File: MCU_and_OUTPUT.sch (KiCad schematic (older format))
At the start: 36 parts, among them P5 CONN_5, P6 CONN_01X04, Q2 BC817-40, Q3 BC817-40, Q4 BC807-40, Q5 IRF540, Q6 BC817-40, SW1 SPST, U2 STM32F030K6, U3 LM358

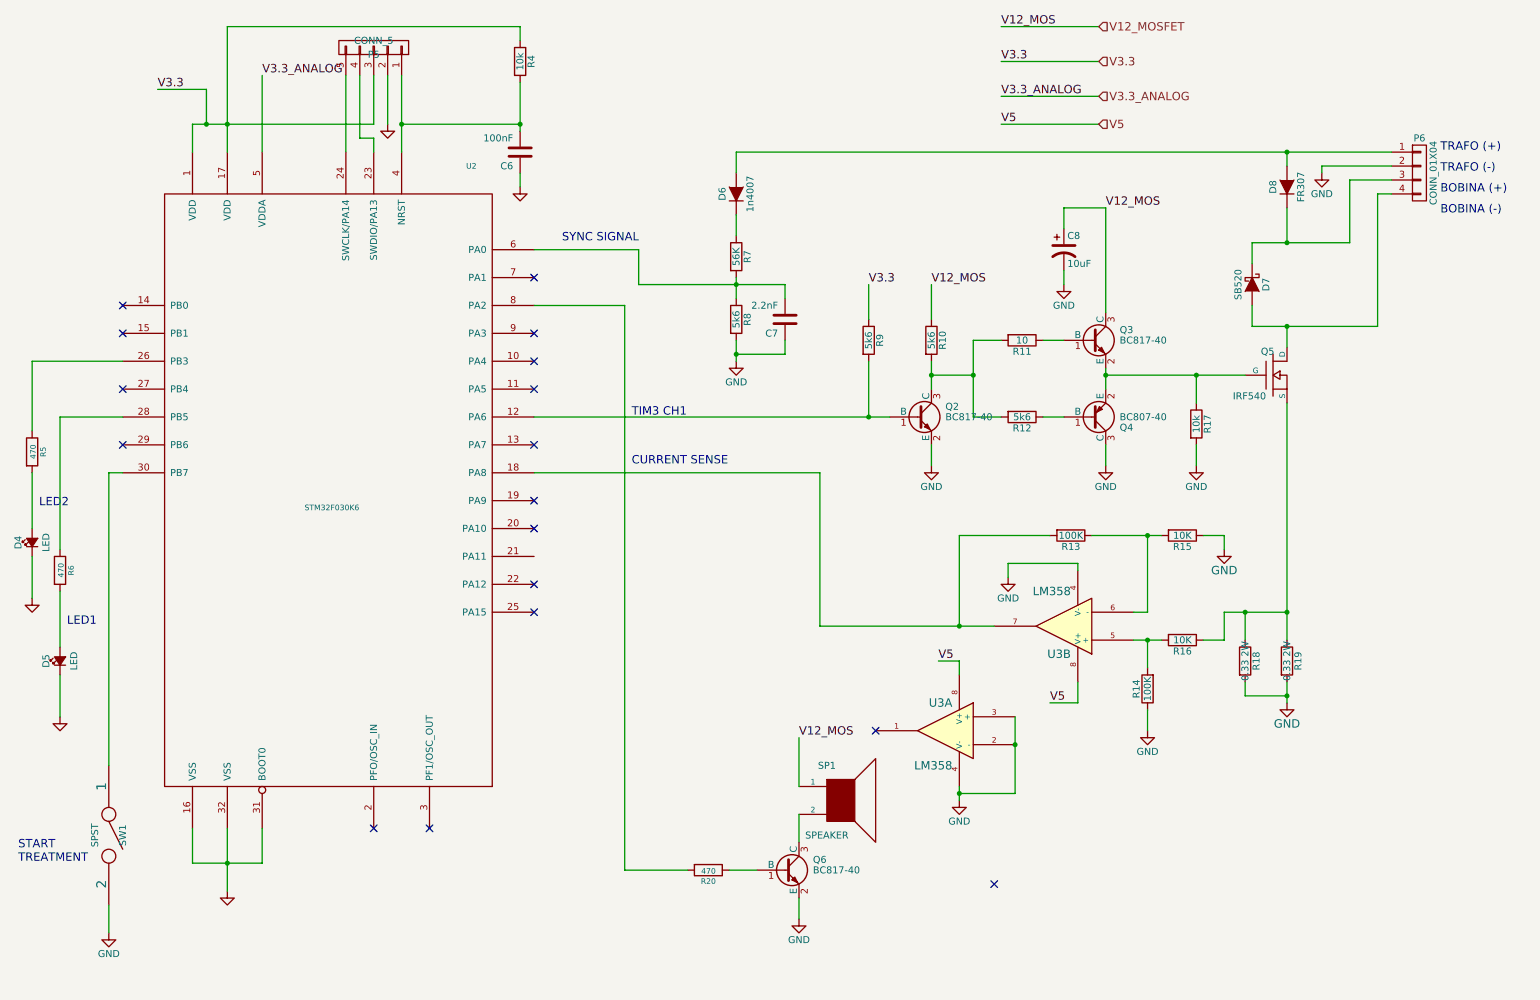
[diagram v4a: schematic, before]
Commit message: mejor ruteo, faltan 3 pistas
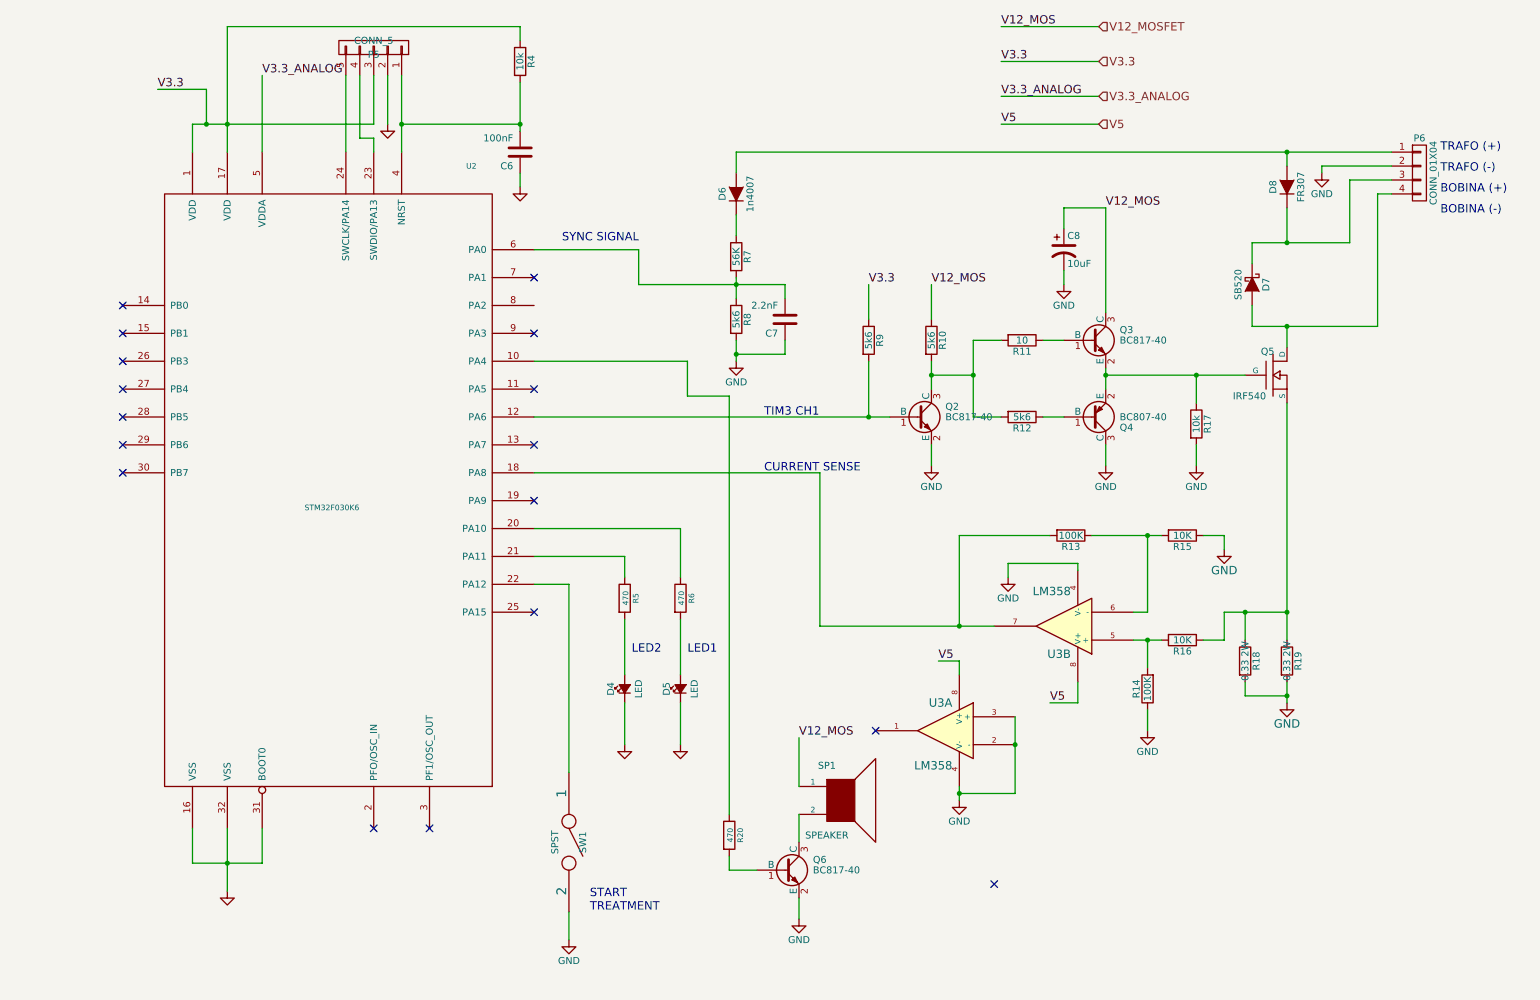
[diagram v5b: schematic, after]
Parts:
- D6: footprint LOCAL_Diode_ThroughHole:Diode_DO-41_SOD81_Horizontal_RM10 -> Diodes_SMD:DO-214AB_Handsoldering
- R17: footprint Resistors_SMD:R_0805_HandSoldering -> Resistors_ThroughHole:Resistor_Horizontal_RM7mm
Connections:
- net at U2.10 (PA4): now also R20.1
- net at U2.20 (PA10): now also R6.1
- net at U2.21 (PA11): now also R5.1
- net at U2.22 (PA12): now also SW1.1
- net at U2.26 (PB3): no longer R5.1
- net at U2.28 (PB5): no longer R6.1
- net at U2.30 (PB7): no longer SW1.1
- net at U2.8 (PA2): no longer R20.2
- net at Q6.1 (B): now also R20.2; no longer R20.1
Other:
- moved on the sheet: D4, D5, R20, R5, R6, SW1
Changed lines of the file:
@@
 L R R5
 U 1 1 56FC59AC
-P 650 3850
-F 0 "R5" V 730 3850 40  0000 C CNN
-F 1 "470" V 657 3851 40  0000 C CNN
-F 2 "Resistors_SMD:R_0805_HandSoldering" V 580 3850 30  0001 C CNN
-F 3 "~" H 650 3850 30  0000 C CNN
-	1    650  3850
+P 4900 4900
+F 0 "R5" V 4980 4900 40  0000 C CNN
+F 1 "470" V 4907 4901 40  0000 C CNN
+F 2 "Resistors_SMD:R_0805_HandSoldering" V 4830 4900 30  0001 C CNN
+F 3 "~" H 4900 4900 30  0000 C CNN
+	1    4900 4900
 	1    0    0    -1
 $EndComp
@@
 L Led_Small D4
 U 1 1 56FC59AD
-P 650 4500
-F 0 "D4" H 650 4600 50  0000 C CNN
-F 1 "LED" H 650 4400 50  0000 C CNN
-F 2 "LEDs:LED-3MM" H 650 4500 60  0001 C CNN
-F 3 "~" H 650 4500 60  0000 C CNN
-	1    650  4500
+P 4900 5550
+F 0 "D4" H 4900 5650 50  0000 C CNN
+F 1 "LED" H 4900 5450 50  0000 C CNN
+F 2 "LEDs:LED-3MM" H 4900 5550 60  0001 C CNN
+F 3 "~" H 4900 5550 60  0000 C CNN
+	1    4900 5550
 	0    -1   -1   0
 $EndComp
@@
 L GND #PWR016
 U 1 1 56FC59AE
-P 650 4900
-F 0 "#PWR016" H 650 4900 30  0001 C CNN
-F 1 "GND" H 650 4830 30  0001 C CNN
-F 2 "" H 650 4900 60  0000 C CNN
-F 3 "" H 650 4900 60  0000 C CNN
-	1    650  4900
+P 4900 5950
+F 0 "#PWR016" H 4900 5950 30  0001 C CNN
+F 1 "GND" H 4900 5880 30  0001 C CNN
+F 2 "" H 4900 5950 60  0000 C CNN
+F 3 "" H 4900 5950 60  0000 C CNN
+	1    4900 5950
 	1    0    0    -1
 $EndComp
@@
 Text Label 7600 1050 0    60   ~ 0
 V3.3
-Text Notes 4950 3600 0    60   ~ 0
+Text Notes 5900 3600 0    60   ~ 0
 TIM3 CH1
 NoConn ~ 1300 2800
@@
 NoConn ~ 4250 3800
 NoConn ~ 4250 3000
-NoConn ~ 4250 3200
 NoConn ~ 4250 3400
 $Comp
 L R R6
 U 1 1 56FC59B2
-P 850 4700
-F 0 "R6" V 930 4700 40  0000 C CNN
-F 1 "470" V 857 4701 40  0000 C CNN
-F 2 "Resistors_SMD:R_0805_HandSoldering" V 780 4700 30  0001 C CNN
-F 3 "~" H 850 4700 30  0000 C CNN
-	1    850  4700
+P 5300 4900
+F 0 "R6" V 5380 4900 40  0000 C CNN
+F 1 "470" V 5307 4901 40  0000 C CNN
+F 2 "Resistors_SMD:R_0805_HandSoldering" V 5230 4900 30  0001 C CNN
+F 3 "~" H 5300 4900 30  0000 C CNN
+	1    5300 4900
 	1    0    0    -1
 $EndComp
@@
 L Led_Small D5
 U 1 1 56FC59B3
-P 850 5350
-F 0 "D5" H 850 5450 50  0000 C CNN
-F 1 "LED" H 850 5250 50  0000 C CNN
-F 2 "LEDs:LED-3MM" H 850 5350 60  0001 C CNN
-F 3 "~" H 850 5350 60  0000 C CNN
-	1    850  5350
+P 5300 5550
+F 0 "D5" H 5300 5650 50  0000 C CNN
+F 1 "LED" H 5300 5450 50  0000 C CNN
+F 2 "LEDs:LED-3MM" H 5300 5550 60  0001 C CNN
+F 3 "~" H 5300 5550 60  0000 C CNN
+	1    5300 5550
 	0    -1   -1   0
 $EndComp
@@
 L GND #PWR018
 U 1 1 56FC59B4
-P 850 5750
-F 0 "#PWR018" H 850 5750 30  0001 C CNN
-F 1 "GND" H 850 5680 30  0001 C CNN
-F 2 "" H 850 5750 60  0000 C CNN
-F 3 "" H 850 5750 60  0000 C CNN
-	1    850  5750
+P 5300 5950
+F 0 "#PWR018" H 5300 5950 30  0001 C CNN
+F 1 "GND" H 5300 5880 30  0001 C CNN
+F 2 "" H 5300 5950 60  0000 C CNN
+F 3 "" H 5300 5950 60  0000 C CNN
+	1    5300 5950
 	1    0    0    -1
 $EndComp
@@
 Text Label 7600 1300 0    60   ~ 0
 V3.3_ANALOG
-Text Notes 900  5100 0    60   ~ 0
+Text Notes 5350 5300 0    60   ~ 0
 LED1
-Text Notes 700  4250 0    60   ~ 0
+Text Notes 4950 5300 0    60   ~ 0
 LED2
 $Comp
@@
 F 0 "R17" V 9080 3650 50  0000 C CNN
 F 1 "10k" V 9000 3650 50  0000 C CNN
-F 2 "Resistors_SMD:R_0805_HandSoldering" V 8930 3650 30  0001 C CNN
+F 2 "Resistors_ThroughHole:Resistor_Horizontal_RM7mm" V 8930 3650 30  0001 C CNN
 F 3 "" H 9000 3650 30  0000 C CNN
 	1    9000 3650
@@
 	3200 1150 3200 1500
 Wire Wire Line
-	3100 1150 3100 1500
+	3100 1500 3100 1150
 Wire Wire Line
 	2050 800  2050 1700
@@
 	1800 1700 1800 1500
 Wire Wire Line
-	2300 6550 2300 6800
-Wire Wire Line
-	2300 6800 1800 6800
+	2300 6800 2300 6550
+Wire Wire Line
+	1800 6800 2300 6800
 Wire Wire Line
 	1800 6800 1800 6550
@@
 Connection ~ 1900 1500
 Wire Wire Line
-	650  4600 650  4900
-Wire Wire Line
-	650  4000 650  4400
+	4900 5650 4900 5950
+Wire Wire Line
+	4900 5050 4900 5450
 Connection ~ 2050 1500
 Wire Wire Line
@@
 	7600 1050 8300 1050
 Wire Wire Line
-	850  5450 850  5750
-Wire Wire Line
-	850  4850 850  5250
+	5300 5650 5300 5950
+Wire Wire Line
+	5300 5050 5300 5450
 Wire Wire Line
 	7600 1300 8300 1300
@@
 	9400 2350 9400 2500
 Wire Wire Line
-	10300 2950 9400 2950
+	9400 2950 10300 2950
 Wire Wire Line
 	9400 2950 9400 2800
@@
 Connection ~ 9650 2350
 Wire Wire Line
-	10300 2000 10300 2950
+	10300 2950 10300 2000
 Wire Wire Line
 	9900 1800 10400 1800
@@
 	10100 2350 9400 2350
 Wire Wire Line
-	10400 2000 10300 2000
+	10300 2000 10400 2000
 $Comp
 L D D6
@@
 F 0 "D6" H 5700 2100 50  0000 C CNN
 F 1 "1n4007" H 5700 1900 50  0000 C CNN
-F 2 "LOCAL_Diode_ThroughHole:Diode_DO-41_SOD81_Horizontal_RM10" H 5700 2000 60  0001 C CNN
+F 2 "Diodes_SMD:DO-214AB_Handsoldering" H 5700 2000 60  0001 C CNN
 F 3 "" H 5700 2000 60  0000 C CNN
 	1    5700 2000
@@
 Text Notes 4450 2350 0    60   ~ 0
 SYNC SIGNAL
-Text Notes 4950 3950 0    60   ~ 0
+Text Notes 5900 4000 0    60   ~ 0
 CURRENT SENSE
 $Comp
@@
 L SPST SW1
 U 1 1 56FFFC2E
-P 1200 6600
-F 0 "SW1" H 1200 6700 50  0000 C CNN
-F 1 "SPST" H 1200 6500 50  0000 C CNN
-F 2 "LOCAL_Pin_Headers:Pin_Header_Straight_1x02" H 1200 6600 60  0001 C CNN
-F 3 "" H 1200 6600 60  0000 C CNN
-	1    1200 6600
+P 4500 6650
+F 0 "SW1" H 4500 6750 50  0000 C CNN
+F 1 "SPST" H 4500 6550 50  0000 C CNN
+F 2 "LOCAL_Pin_Headers:Pin_Header_Straight_1x02" H 4500 6650 60  0001 C CNN
+F 3 "" H 4500 6650 60  0000 C CNN
+	1    4500 6650
 	0    1    1    0
 $EndComp
@@
 L GND #PWR031
 U 1 1 57000B38
-P 1200 7300
-F 0 "#PWR031" H 1200 7050 50  0001 C CNN
-F 1 "GND" H 1200 7150 50  0000 C CNN
-F 2 "" H 1200 7300 60  0000 C CNN
-F 3 "" H 1200 7300 60  0000 C CNN
-	1    1200 7300
+P 4500 7350
+F 0 "#PWR031" H 4500 7100 50  0001 C CNN
+F 1 "GND" H 4500 7200 50  0000 C CNN
+F 2 "" H 4500 7350 60  0000 C CNN
+F 3 "" H 4500 7350 60  0000 C CNN
+	1    4500 7350
 	1    0    0    -1
 $EndComp
@@
 L R R20
 U 1 1 5700128D
-P 5500 6850
-F 0 "R20" V 5580 6850 40  0000 C CNN
-F 1 "470" V 5507 6851 40  0000 C CNN
-F 2 "Resistors_SMD:R_0805_HandSoldering" V 5430 6850 30  0001 C CNN
-F 3 "~" H 5500 6850 30  0000 C CNN
-	1    5500 6850
-	0    1    1    0
-$EndComp
-Wire Wire Line
-	4900 2800 4900 6850
-Wire Wire Line
-	4900 6850 5350 6850
+P 5650 6600
+F 0 "R20" V 5730 6600 40  0000 C CNN
+F 1 "470" V 5657 6601 40  0000 C CNN
+F 2 "Resistors_SMD:R_0805_HandSoldering" V 5580 6600 30  0001 C CNN
+F 3 "~" H 5650 6600 30  0000 C CNN
+	1    5650 6600
+	1    0    0    -1
+$EndComp
 Wire Wire Line
 	5650 6850 5850 6850
-Text Notes 550  6800 0    60   ~ 0
+Text Notes 4650 7150 0    60   ~ 0
 START\nTREATMENT
 NoConn ~ 4250 4200
-NoConn ~ 4250 4400
 $Comp
 L STM32F030K6 U2
@@
 	1    0    0    -1
 $EndComp
-NoConn ~ 4250 4800
-Wire Wire Line
-	1300 4000 1200 4000
-Wire Wire Line
-	1200 4000 1200 6100
-Wire Wire Line
-	1200 7100 1200 7300
-Wire Wire Line
-	1300 3600 850  3600
-Wire Wire Line
-	850  3600 850  4550
-Wire Wire Line
-	1300 3200 650  3200
-Wire Wire Line
-	650  3200 650  3700
+Wire Wire Line
+	4500 7150 4500 7350
 NoConn ~ 1300 3400
 NoConn ~ 1300 3800
 Wire Wire Line
-	4900 2800 4250 2800
+	5650 6850 5650 6750
+Wire Wire Line
+	5650 6450 5650 3450
+Wire Wire Line
+	5650 3450 5350 3450
+NoConn ~ 1300 4000
+NoConn ~ 1300 3200
+NoConn ~ 1300 3600
+Wire Wire Line
+	4250 4800 4500 4800
+Wire Wire Line
+	4500 4800 4500 6150
+Wire Wire Line
+	4250 4600 4900 4600
+Wire Wire Line
+	4900 4600 4900 4750
+Wire Wire Line
+	4250 4400 5300 4400
+Wire Wire Line
+	5300 4400 5300 4750
+Wire Wire Line
+	5350 3450 5350 3200
+Wire Wire Line
+	5350 3200 4250 3200
 $EndSCHEMATC

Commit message: todo termiando con plano de masa y pines .2
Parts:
- P6: footprint LOCAL_Pin_Headers:Pin_Header_Straight_1x04 -> LOCAL_Connect:bornier4
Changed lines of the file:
@@
 F 0 "P6" H 10600 2100 50  0000 C CNN
 F 1 "CONN_01X04" V 10700 1850 50  0000 C CNN
-F 2 "LOCAL_Pin_Headers:Pin_Header_Straight_1x04" H 10600 1850 60  0001 C CNN
+F 2 "LOCAL_Connect:bornier4" H 10600 1850 60  0001 C CNN
 F 3 "" H 10600 1850 60  0000 C CNN
 	1    10600 1850
